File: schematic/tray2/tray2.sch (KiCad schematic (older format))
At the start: 59 parts, among them J1 AVR-ISP-10, J2 Conn_02x10_Odd_Even, J3 Conn_Coaxial, J4 Conn_Coaxial, J5 Conn_Coaxial, Q1 BF998, Q2 BFP196, Q3 BFR92A, Q4 BFR92A, U1 74AC253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

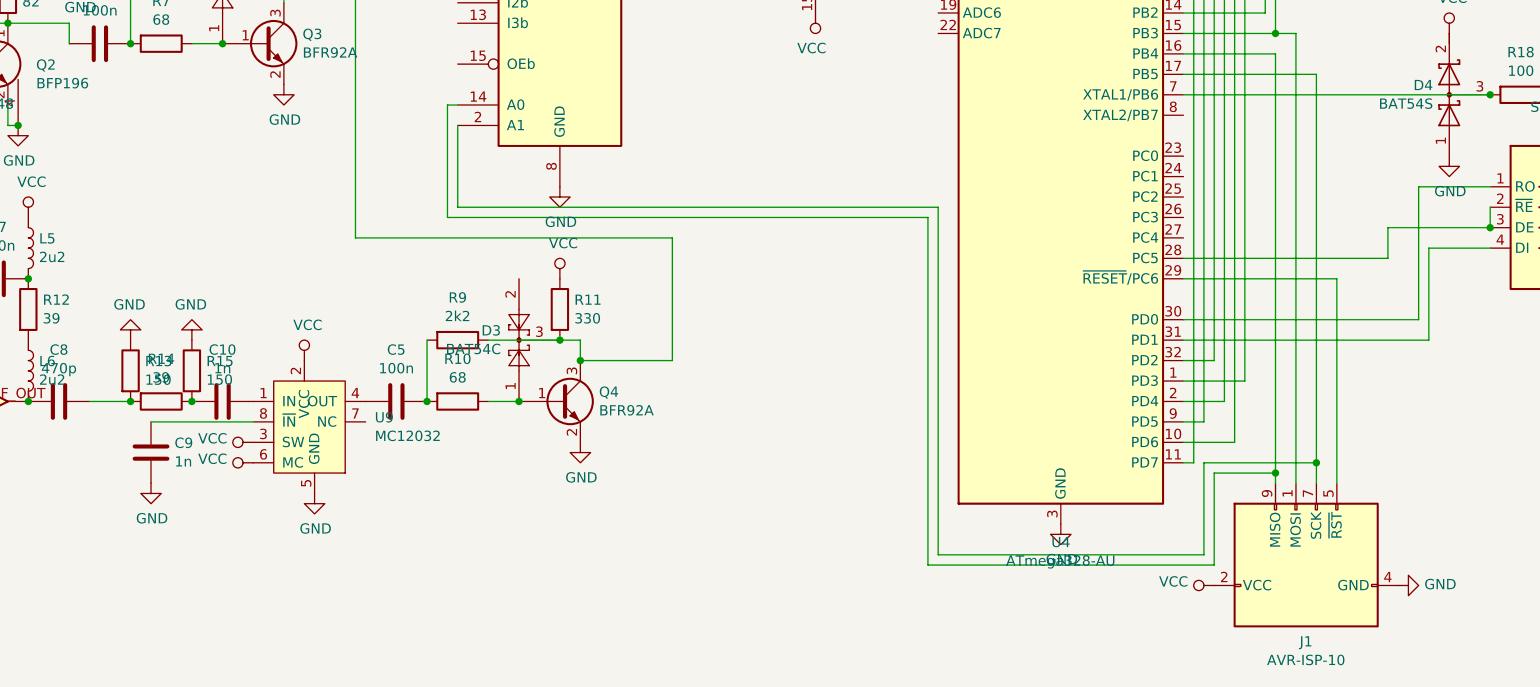
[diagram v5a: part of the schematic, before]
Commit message: Use tested MB506 prescaler
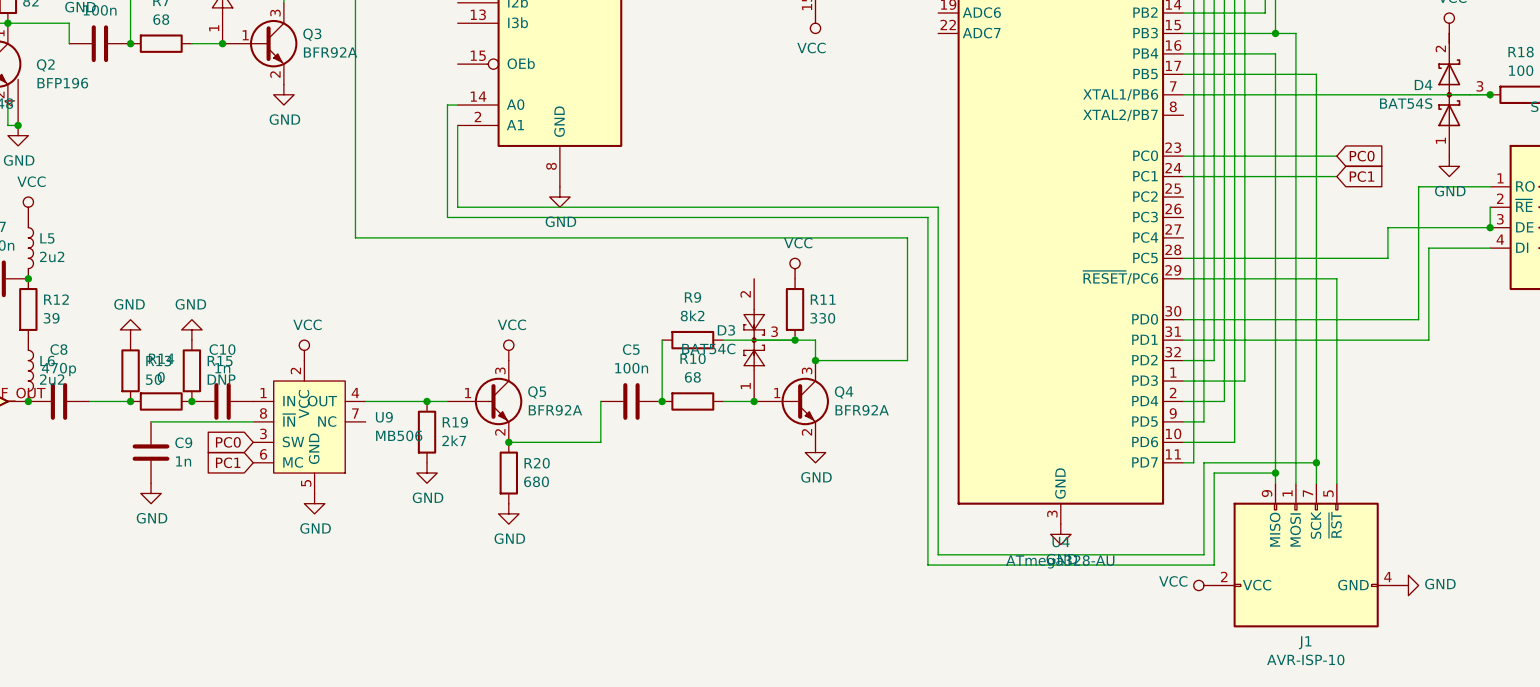
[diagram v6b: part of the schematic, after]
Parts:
- added Q5: BFR92A, Package_TO_SOT_SMD:SOT-23, symbol Transistor_BJT:BFR92
- added R19: 2k7, Resistor_SMD:R_0805_2012Metric_Pad1.15x1.40mm_HandSolder, symbol Device:R
- added R20: 680, Resistor_SMD:R_0805_2012Metric_Pad1.15x1.40mm_HandSolder, symbol Device:R
- R13: value 150 -> 50
- R14: value 39 -> 0
- R15: value 150 -> DNP
- R9: value 2k2 -> 8k2
- U9: value MC12032 -> MB506; footprint Package_SO:SO-8_3.9x4.9mm_P1.27mm -> Package_SO:SO-8_5.3x6.2mm_P1.27mm
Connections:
- net GND: now also R19.2, R20.2
- net VCC: now also Q5.3 (C); no longer U9.3 (SW), U9.6 (MC)
- net PC0: now reaches U4.23 (PC0)
- net PC0: now also U9.3 (SW)
- net PC1: now reaches U4.24 (PC1)
- net PC1: now also U9.6 (MC)
- net at C5.2: now also Q5.2 (E), R20.1; no longer U9.4 (OUT)
- new net: Q5.1 (B), R19.1, U9.4 (OUT)
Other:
- moved on the sheet: C5, D3, Q4, R10, R11, R9
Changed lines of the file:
@@
 L Transistor_BJT:BC847 Q4
 U 1 1 5E191631
-P 4700 5400
-F 0 "Q4" H 4891 5446 50  0000 L CNN
-F 1 "BFR92A" H 4891 5355 50  0000 L CNN
-F 2 "Package_TO_SOT_SMD:SOT-23" H 4900 5325 50  0001 L CIN
-F 3 "http://www.infineon.com/dgdl/Infineon-BC847SERIES_BC848SERIES_BC849SERIES_BC850SERIES-DS-v01_01-en.pdf?fileId=db3a304314dca389011541d4630a1657" H 4700 5400 50  0001 L CNN
-	1    4700 5400
+P 5850 5400
+F 0 "Q4" H 6041 5446 50  0000 L CNN
+F 1 "BFR92A" H 6041 5355 50  0000 L CNN
+F 2 "Package_TO_SOT_SMD:SOT-23" H 6050 5325 50  0001 L CIN
+F 3 "http://www.infineon.com/dgdl/Infineon-BC847SERIES_BC848SERIES_BC849SERIES_BC850SERIES-DS-v01_01-en.pdf?fileId=db3a304314dca389011541d4630a1657" H 5850 5400 50  0001 L CNN
+	1    5850 5400
 	1    0    0    -1
 $EndComp
@@
 L Diode:BAT54C D3
 U 1 1 5E191637
-P 4500 5100
-F 0 "D3" V 4546 5188 50  0000 L CNN
-F 1 "BAT54C" V 4455 5188 50  0000 L CNN
-F 2 "Package_TO_SOT_SMD:SOT-23" H 4575 5225 50  0001 L CNN
-F 3 "http://www.diodes.com/_files/datasheets/ds11005.pdf" H 4420 5100 50  0001 C CNN
-	1    4500 5100
+P 5650 5100
+F 0 "D3" V 5696 5188 50  0000 L CNN
+F 1 "BAT54C" V 5605 5188 50  0000 L CNN
+F 2 "Package_TO_SOT_SMD:SOT-23" H 5725 5225 50  0001 L CNN
+F 3 "http://www.diodes.com/_files/datasheets/ds11005.pdf" H 5570 5100 50  0001 C CNN
+	1    5650 5100
 	0    -1   -1   0
 $EndComp
@@
 L Device:C C5
 U 1 1 5E19163D
-P 3900 5400
-F 0 "C5" V 3648 5400 50  0000 C CNN
-F 1 "100n" V 3739 5400 50  0000 C CNN
-F 2 "Capacitor_SMD:C_0805_2012Metric" H 3938 5250 50  0001 C CNN
-F 3 "~" H 3900 5400 50  0001 C CNN
-	1    3900 5400
+P 5050 5400
+F 0 "C5" V 4798 5400 50  0000 C CNN
+F 1 "100n" V 4889 5400 50  0000 C CNN
+F 2 "Capacitor_SMD:C_0805_2012Metric" H 5088 5250 50  0001 C CNN
+F 3 "~" H 5050 5400 50  0001 C CNN
+	1    5050 5400
 	0    1    1    0
 $EndComp
 Wire Wire Line
-	4500 5400 4350 5400
-Connection ~ 4500 5400
+	5650 5400 5500 5400
+Connection ~ 5650 5400
 $Comp
 L Device:R R10
 U 1 1 5E191645
-P 4200 5400
-F 0 "R10" V 3993 5400 50  0000 C CNN
-F 1 "68" V 4084 5400 50  0000 C CNN
-F 2 "Resistor_SMD:R_0805_2012Metric" V 4130 5400 50  0001 C CNN
-F 3 "~" H 4200 5400 50  0001 C CNN
-	1    4200 5400
+P 5350 5400
+F 0 "R10" V 5143 5400 50  0000 C CNN
+F 1 "68" V 5234 5400 50  0000 C CNN
+F 2 "Resistor_SMD:R_0805_2012Metric" V 5280 5400 50  0001 C CNN
+F 3 "~" H 5350 5400 50  0001 C CNN
+	1    5350 5400
 	0    1    1    0
 $EndComp
@@
 L Device:R R9
 U 1 1 5E19164B
-P 4200 5100
-F 0 "R9" V 3993 5100 50  0000 C CNN
-F 1 "2k2" V 4084 5100 50  0000 C CNN
-F 2 "Resistor_SMD:R_0805_2012Metric" V 4130 5100 50  0001 C CNN
-F 3 "~" H 4200 5100 50  0001 C CNN
-	1    4200 5100
+P 5350 5100
+F 0 "R9" V 5143 5100 50  0000 C CNN
+F 1 "8k2" V 5234 5100 50  0000 C CNN
+F 2 "Resistor_SMD:R_0805_2012Metric" V 5280 5100 50  0001 C CNN
+F 3 "~" H 5350 5100 50  0001 C CNN
+	1    5350 5100
 	0    1    1    0
 $EndComp
 Wire Wire Line
-	4050 5400 4050 5100
-Connection ~ 4050 5400
-Wire Wire Line
-	4350 5100 4700 5100
-Wire Wire Line
-	4700 5100 4800 5100
-Wire Wire Line
-	4800 5100 4800 5200
-Connection ~ 4700 5100
+	5200 5400 5200 5100
+Connection ~ 5200 5400
+Wire Wire Line
+	5500 5100 5850 5100
+Wire Wire Line
+	5850 5100 5950 5100
+Wire Wire Line
+	5950 5100 5950 5200
+Connection ~ 5850 5100
 $Comp
 L Device:R R11
 U 1 1 5E191657
-P 4700 4950
-F 0 "R11" H 4770 4996 50  0000 L CNN
-F 1 "330" H 4770 4905 50  0000 L CNN
-F 2 "Resistor_SMD:R_0805_2012Metric" V 4630 4950 50  0001 C CNN
-F 3 "~" H 4700 4950 50  0001 C CNN
-	1    4700 4950
+P 5850 4950
+F 0 "R11" H 5920 4996 50  0000 L CNN
+F 1 "330" H 5920 4905 50  0000 L CNN
+F 2 "Resistor_SMD:R_0805_2012Metric" V 5780 4950 50  0001 C CNN
+F 3 "~" H 5850 4950 50  0001 C CNN
+	1    5850 4950
 	1    0    0    -1
 $EndComp
@@
 L power:VCC #PWR025
 U 1 1 5E19165D
-P 4700 4800
-F 0 "#PWR025" H 4700 4650 50  0001 C CNN
-F 1 "VCC" H 4717 4973 50  0000 C CNN
-F 2 "" H 4700 4800 50  0001 C CNN
-F 3 "" H 4700 4800 50  0001 C CNN
-	1    4700 4800
+P 5850 4800
+F 0 "#PWR025" H 5850 4650 50  0001 C CNN
+F 1 "VCC" H 5867 4973 50  0000 C CNN
+F 2 "" H 5850 4800 50  0001 C CNN
+F 3 "" H 5850 4800 50  0001 C CNN
+	1    5850 4800
 	1    0    0    -1
 $EndComp
@@
 L power:GND #PWR026
 U 1 1 5E191663
-P 4800 5600
-F 0 "#PWR026" H 4800 5350 50  0001 C CNN
-F 1 "GND" H 4805 5427 50  0000 C CNN
-F 2 "" H 4800 5600 50  0001 C CNN
-F 3 "" H 4800 5600 50  0001 C CNN
-	1    4800 5600
-	1    0    0    -1
-$EndComp
-Wire Wire Line
-	5250 5200 4800 5200
-Connection ~ 4800 5200
-Wire Wire Line
-	5250 5200 5250 4600
-Wire Wire Line
-	5250 4600 3700 4600
+P 5950 5600
+F 0 "#PWR026" H 5950 5350 50  0001 C CNN
+F 1 "GND" H 5955 5427 50  0000 C CNN
+F 2 "" H 5950 5600 50  0001 C CNN
+F 3 "" H 5950 5600 50  0001 C CNN
+	1    5950 5600
+	1    0    0    -1
+$EndComp
+Wire Wire Line
+	6400 5200 5950 5200
+Connection ~ 5950 5200
+Wire Wire Line
+	6400 5200 6400 4600
 $Comp
 L Connector:Conn_Coaxial J5
@@
 P 3450 6050
 F 0 "U9" H 3794 6621 50  0000 L CNN
-F 1 "MC12032" H 3794 6530 50  0000 L CNN
-F 2 "Package_SO:SO-8_3.9x4.9mm_P1.27mm" H 3450 6050 50  0001 C CNN
+F 1 "MB506" H 3794 6530 50  0000 L CNN
+F 2 "Package_SO:SO-8_5.3x6.2mm_P1.27mm" H 3450 6050 50  0001 C CNN
 F 3 "" H 3450 6050 50  0001 C CNN
 	1    3450 6050
@@
 	1    3450 5200
 	1    0    0    -1
-$EndComp
-$Comp
-L power:VCC #PWR034
-U 1 1 5E214394
-P 3200 5600
-F 0 "#PWR034" H 3200 5450 50  0001 C CNN
-F 1 "VCC" V 3218 5727 50  0000 L CNN
-F 2 "" H 3200 5600 50  0001 C CNN
-F 3 "" H 3200 5600 50  0001 C CNN
-	1    3200 5600
-	0    -1   -1   0
-$EndComp
-$Comp
-L power:VCC #PWR035
-U 1 1 5E215055
-P 3200 5700
-F 0 "#PWR035" H 3200 5550 50  0001 C CNN
-F 1 "VCC" V 3218 5827 50  0000 L CNN
-F 2 "" H 3200 5700 50  0001 C CNN
-F 3 "" H 3200 5700 50  0001 C CNN
-	1    3200 5700
-	0    -1   -1   0
 $EndComp
 $Comp
@@
 P 2750 5400
 F 0 "R14" V 2543 5400 50  0000 C CNN
-F 1 "39" V 2634 5400 50  0000 C CNN
+F 1 "0" V 2634 5400 50  0000 C CNN
 F 2 "Resistor_SMD:R_0805_2012Metric" V 2680 5400 50  0001 C CNN
 F 3 "~" H 2750 5400 50  0001 C CNN
@@
 P 2900 5250
 F 0 "R15" H 2970 5296 50  0000 L CNN
-F 1 "150" H 2970 5205 50  0000 L CNN
+F 1 "DNP" H 2970 5205 50  0000 L CNN
 F 2 "Resistor_SMD:R_0805_2012Metric" V 2830 5250 50  0001 C CNN
 F 3 "~" H 2900 5250 50  0001 C CNN
@@
 P 2600 5250
 F 0 "R13" H 2670 5296 50  0000 L CNN
-F 1 "150" H 2670 5205 50  0000 L CNN
+F 1 "50" H 2670 5205 50  0000 L CNN
 F 2 "Resistor_SMD:R_0805_2012Metric" V 2530 5250 50  0001 C CNN
 F 3 "~" H 2600 5250 50  0001 C CNN
@@
 Wire Wire Line
 	10050 3900 9550 3900
+Wire Wire Line
+	3700 4600 6400 4600
+Wire Wire Line
+	4150 5400 4050 5400
+$Comp
+L power:VCC #PWR045
+U 1 1 5EB3036C
+P 4450 5200
+F 0 "#PWR045" H 4450 5050 50  0001 C CNN
+F 1 "VCC" H 4467 5373 50  0000 C CNN
+F 2 "" H 4450 5200 50  0001 C CNN
+F 3 "" H 4450 5200 50  0001 C CNN
+	1    4450 5200
+	1    0    0    -1
+$EndComp
+$Comp
+L Device:R R20
+U 1 1 5EB31393
+P 4450 5750
+F 0 "R20" H 4520 5796 50  0000 L CNN
+F 1 "680" H 4520 5705 50  0000 L CNN
+F 2 "Resistor_SMD:R_0805_2012Metric_Pad1.15x1.40mm_HandSolder" V 4380 5750 50  0001 C CNN
+F 3 "~" H 4450 5750 50  0001 C CNN
+	1    4450 5750
+	1    0    0    -1
+$EndComp
+$Comp
+L Device:R R19
+U 1 1 5EB31EFF
+P 4050 5550
+F 0 "R19" H 4120 5596 50  0000 L CNN
+F 1 "2k7" H 4120 5505 50  0000 L CNN
+F 2 "Resistor_SMD:R_0805_2012Metric_Pad1.15x1.40mm_HandSolder" V 3980 5550 50  0001 C CNN
+F 3 "~" H 4050 5550 50  0001 C CNN
+	1    4050 5550
+	1    0    0    -1
+$EndComp
+Connection ~ 4050 5400
+Wire Wire Line
+	4050 5400 3750 5400
+$Comp
+L power:GND #PWR044
+U 1 1 5EB33497
+P 4050 5700
+F 0 "#PWR044" H 4050 5450 50  0001 C CNN
+F 1 "GND" H 4055 5527 50  0000 C CNN
+F 2 "" H 4050 5700 50  0001 C CNN
+F 3 "" H 4050 5700 50  0001 C CNN
+	1    4050 5700
+	1    0    0    -1
+$EndComp
+$Comp
+L power:GND #PWR046
+U 1 1 5EB34107
+P 4450 5900
+F 0 "#PWR046" H 4450 5650 50  0001 C CNN
+F 1 "GND" H 4455 5727 50  0000 C CNN
+F 2 "" H 4450 5900 50  0001 C CNN
+F 3 "" H 4450 5900 50  0001 C CNN
+	1    4450 5900
+	1    0    0    -1
+$EndComp
+$Comp
+L Transistor_BJT:BFR92 Q5
+U 1 1 5EB28DFD
+P 4350 5400
+F 0 "Q5" H 4541 5446 50  0000 L CNN
+F 1 "BFR92A" H 4541 5355 50  0000 L CNN
+F 2 "Package_TO_SOT_SMD:SOT-23" H 4550 5325 50  0001 L CIN
+F 3 "https://assets.nexperia.com/documents/data-sheet/BFR92A_N.pdf" H 4350 5400 50  0001 L CNN
+	1    4350 5400
+	1    0    0    -1
+$EndComp
+Wire Wire Line
+	4900 5400 4900 5600
+Wire Wire Line
+	4900 5600 4450 5600
+Connection ~ 4450 5600
+Wire Wire Line
+	8500 4200 7750 4200
+Wire Wire Line
+	8500 4300 7750 4300
+Text GLabel 8500 4200 2    50   Input ~ 0
+PC0
+Text GLabel 8500 4300 2    50   Input ~ 0
+PC1
+Text GLabel 3200 5600 0    50   Input ~ 0
+PC0
+Text GLabel 3200 5700 0    50   Input ~ 0
+PC1
 $EndSCHEMATC

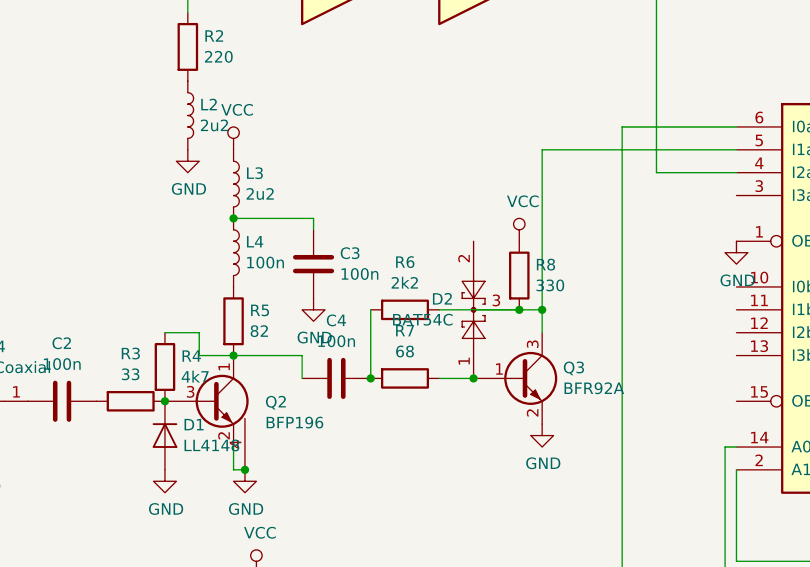
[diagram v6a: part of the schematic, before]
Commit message: In HF change resistor so it works better with CMOS inputs - now working up to 100MHz before 90MHz
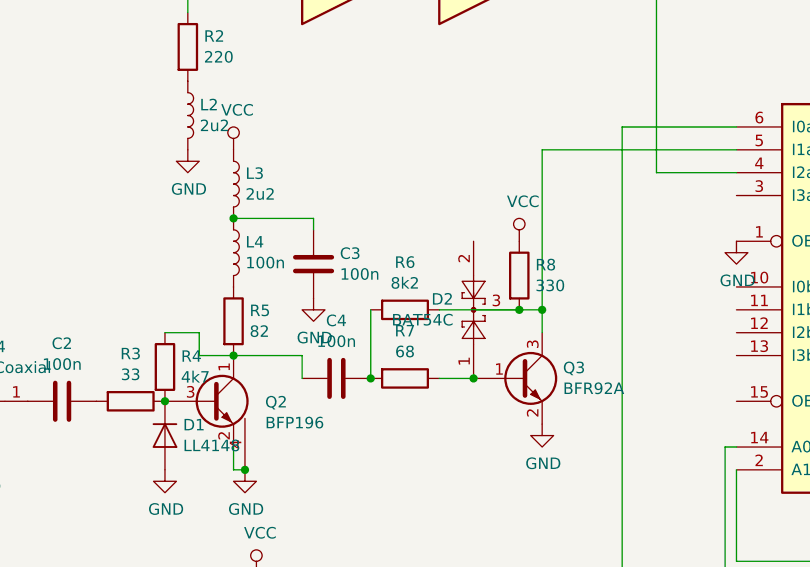
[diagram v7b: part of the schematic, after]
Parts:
- R6: value 2k2 -> 8k2
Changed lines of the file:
@@
 P 2750 3350
 F 0 "R6" V 2543 3350 50  0000 C CNN
-F 1 "2k2" V 2634 3350 50  0000 C CNN
+F 1 "8k2" V 2634 3350 50  0000 C CNN
 F 2 "Resistor_SMD:R_0805_2012Metric" V 2680 3350 50  0001 C CNN
 F 3 "~" H 2750 3350 50  0001 C CNN
